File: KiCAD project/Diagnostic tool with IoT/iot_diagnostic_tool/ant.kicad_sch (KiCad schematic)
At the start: 8 parts

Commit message: Update 06/03/23 - new board layout WIP 70%
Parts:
- AE1, AE2: footprint (none) -> Connector_Coaxial:U.FL_Hirose_U.FL-R-SMT-1_Vertical
- C38, C39, C40, C41: footprint (none) -> Capacitor_SMD:C_0402_1005Metric
- R38, R39: footprint (none) -> Resistor_SMD:R_0402_1005Metric
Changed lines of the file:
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@@
       (effects (font (size 1.27 1.27)) (justify left))
     )
-    (property "Footprint" "" (at 97.4852 101.6 0)
+    (property "Footprint" "Capacitor_SMD:C_0402_1005Metric" (at 97.4852 101.6 0)
       (effects (font (size 1.27 1.27)) hide)
     )
@@
       (effects (font (size 1.27 1.27)))
     )
-    (property "Footprint" "" (at 177.8 95.758 90)
+    (property "Footprint" "Resistor_SMD:R_0402_1005Metric" (at 177.8 95.758 90)
       (effects (font (size 1.27 1.27)) hide)
     )
@@
       (effects (font (size 1.27 1.27)) (justify left))
     )
-    (property "Footprint" "" (at 168.6052 101.6 0)
+    (property "Footprint" "Capacitor_SMD:C_0402_1005Metric" (at 168.6052 101.6 0)
       (effects (font (size 1.27 1.27)) hide)
     )
@@
       (effects (font (size 1.27 1.27)))
     )
-    (property "Footprint" "" (at 106.68 95.758 90)
+    (property "Footprint" "Resistor_SMD:R_0402_1005Metric" (at 106.68 95.758 90)
       (effects (font (size 1.27 1.27)) hide)
     )
@@
       (effects (font (size 1.27 1.27)) (justify left))
     )
-    (property "Footprint" "" (at 117.8052 101.6 0)
+    (property "Footprint" "Capacitor_SMD:C_0402_1005Metric" (at 117.8052 101.6 0)
       (effects (font (size 1.27 1.27)) hide)
     )
@@
       (effects (font (size 1.27 1.27)) (justify left))
     )
-    (property "Footprint" "" (at 188.9252 101.6 0)
+    (property "Footprint" "Capacitor_SMD:C_0402_1005Metric" (at 188.9252 101.6 0)
       (effects (font (size 1.27 1.27)) hide)
     )
@@
       (effects (font (size 1.27 1.27)) (justify left))
     )
-    (property "Footprint" "" (at 202.565 88.9 0)
+    (property "Footprint" "Connector_Coaxial:U.FL_Hirose_U.FL-R-SMT-1_Vertical" (at 202.565 88.9 0)
       (effects (font (size 1.27 1.27)) hide)
     )
@@
       (effects (font (size 1.27 1.27)) (justify left))
     )
-    (property "Footprint" "" (at 131.445 88.9 0)
-      (effects (font (size 1.27 1.27)) hide)
-    )
+    (property "Footprint" "Connector_Coaxial:U.FL_Hirose_U.FL-R-SMT-1_Vertical" (at 131.445 88.9 0)
+      (effects (font (size 1.27 1.27)) hide)
+    )

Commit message: Update 07/03/23 - board layout done
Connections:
- net ANT_GNSS: now also AE2.1 (A), C41.1, R39.2
- net ANT_MAIN: now also AE1.1 (A), C39.1, R38.2
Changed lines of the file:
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@@
     (effects (font (size 5 5) bold) (justify left bottom))
+  )
+  (label "ANT_MAIN" (at 116.84 93.98 0) (fields_autoplaced)
+    (effects (font (size 1.27 1.27)) (justify left bottom))
+  )
+  (label "ANT_GNSS" (at 187.96 93.98 0) (fields_autoplaced)
+    (effects (font (size 1.27 1.27)) (justify left bottom))
   )
   (global_label "ANT_GNSS" (shape input) (at 161.29 93.98 180) (fields_autoplaced)

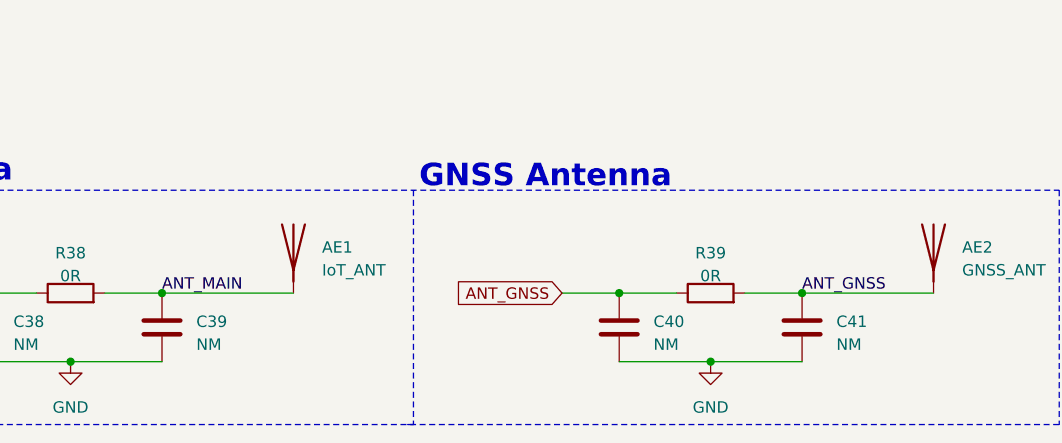
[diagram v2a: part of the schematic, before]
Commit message: Update 13/03/23 - Board layout fixes
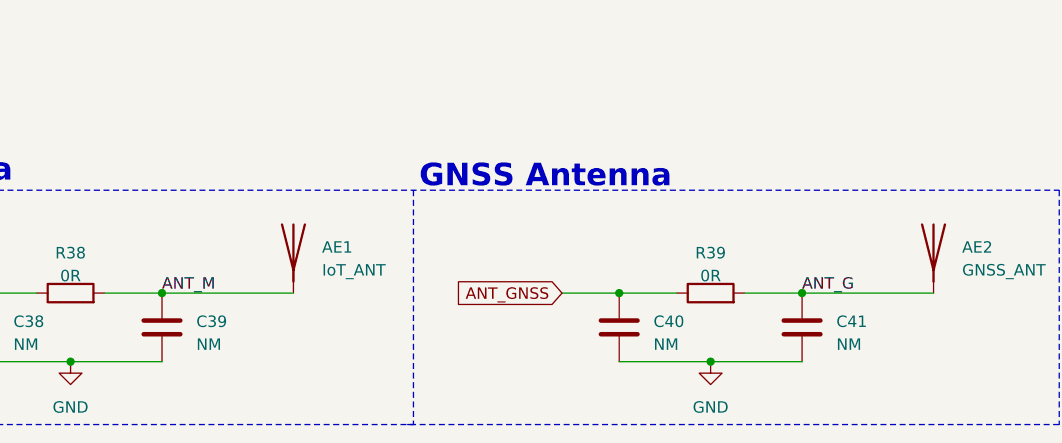
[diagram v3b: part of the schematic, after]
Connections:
- net ANT_GNSS: no longer AE2.1 (A), C41.1, R39.2
- net ANT_MAIN: no longer AE1.1 (A), C39.1, R38.2
- new net ANT_G: AE2.1 (A), C41.1, R39.2
- new net ANT_M: AE1.1 (A), C39.1, R38.2
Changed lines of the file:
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@@
     (effects (font (size 5 5) bold) (justify left bottom))
   )
-  (label "ANT_MAIN" (at 116.84 93.98 0) (fields_autoplaced)
+  (label "ANT_M" (at 116.84 93.98 0) (fields_autoplaced)
     (effects (font (size 1.27 1.27)) (justify left bottom))
   )
-  (label "ANT_GNSS" (at 187.96 93.98 0) (fields_autoplaced)
+  (label "ANT_G" (at 187.96 93.98 0) (fields_autoplaced)
     (effects (font (size 1.27 1.27)) (justify left bottom))
   )

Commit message: Update 26/06/23 - Thesis release
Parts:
- added C26: 100p, symbol Device:C
- added C30: 100n, symbol Device:C
- added L2: 47n, symbol Device:L
- added R23: 10R, symbol Device:R
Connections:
- net ANT_G: no longer AE2.1 (A)
- net GND: now also C30.2
- new net: AE2.1 (A), C26.2, L2.2
- new net: L2.1, R23.2
- new net +3V3: C30.1, R23.1
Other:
- company: (none) -> FEKT VUT
- title: (none) -> OBD Monitoring Device
- moved on the sheet: AE1, AE2, C38, C39, C40, C41, R38, R39
